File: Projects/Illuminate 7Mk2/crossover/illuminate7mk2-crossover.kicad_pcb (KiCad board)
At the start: 2 copper layers, 202.2 x 179.2 mm, 27 parts, among them J1 IN (amp), J2 TWEETER, J3 WOOFER

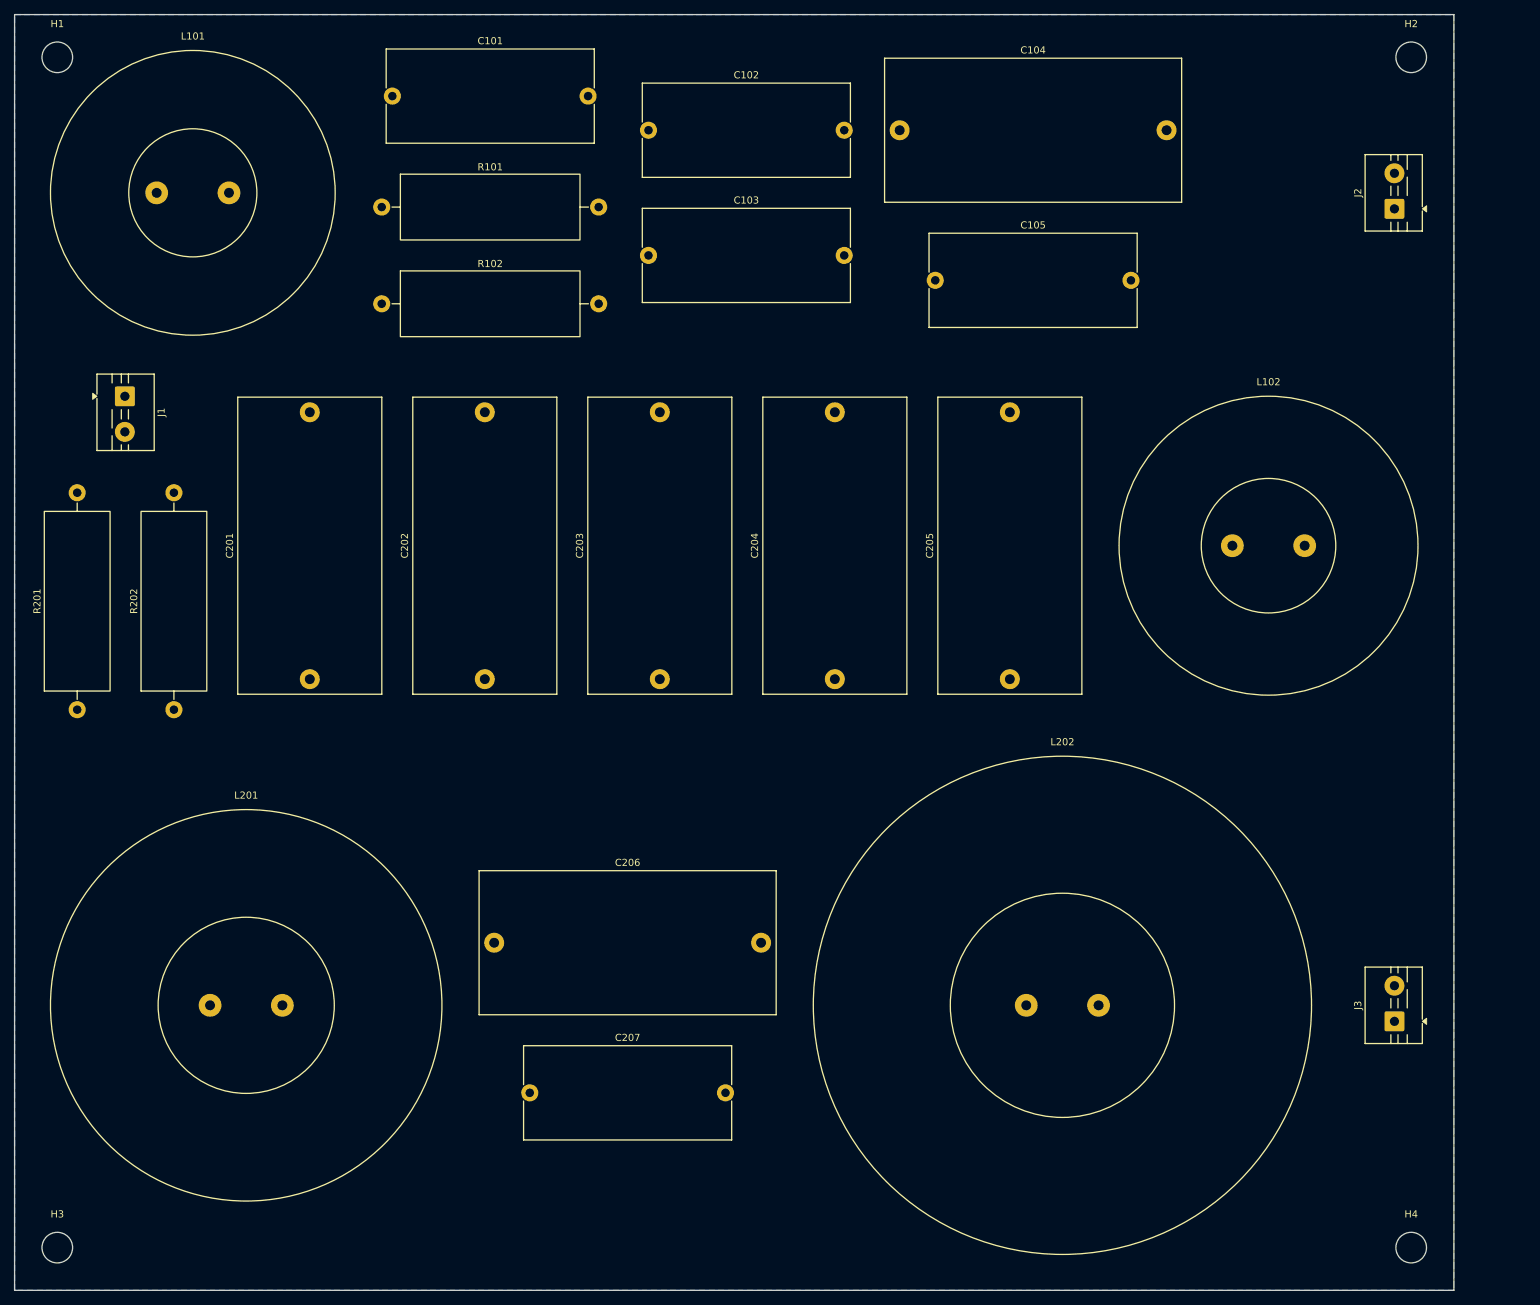
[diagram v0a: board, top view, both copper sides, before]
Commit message: Illuminate 7Mk2: crossover board shrunk to the mill envelope
Coils moved off the board: only their lead pads remain, at the edges.
Board is now 167 x 144 mm, inside the 203 x 152 mm build size.
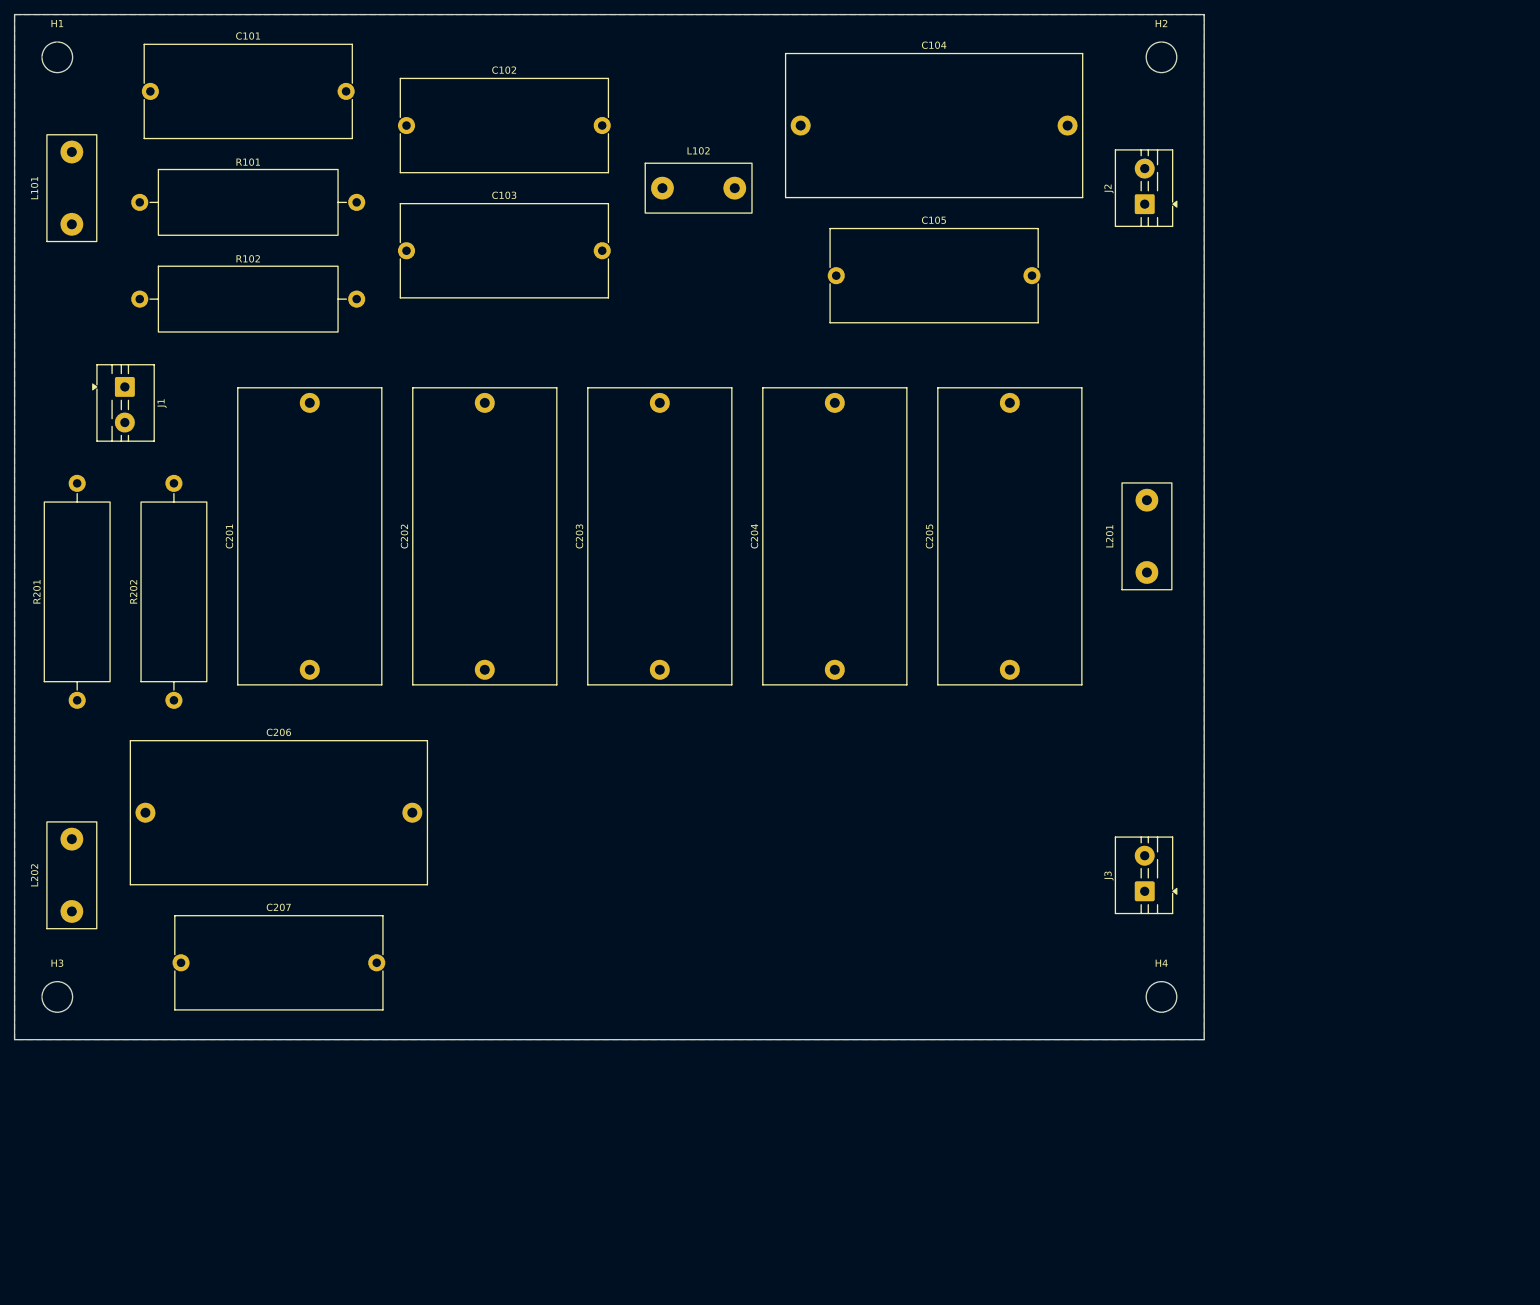
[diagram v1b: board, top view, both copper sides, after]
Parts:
- L101: footprint L_AirCore_D40mm_0.8mm -> L_OffBoard_P10.16mm
- L102: footprint L_AirCore_D42mm_0.8mm -> L_OffBoard_P10.16mm
- L201: footprint L_AirCore_D55mm_0.8mm -> L_OffBoard_P10.16mm
- L202: footprint L_AirCore_D70mm_0.8mm -> L_OffBoard_P10.16mm
- moved L201 142.7 mm to (159.1, 73.3), turned to 90 degrees
- moved L202 140.4 mm to (8.04, 120.9), turned to 90 degrees
- moved L102 94.5 mm to (96.1, 24.4)
- moved C206 52.3 mm to (18.4, 112.1)
- moved C207 52.3 mm to (23.4, 133.2)
- moved H4 49.7 mm to (161.1, 138.0)
- moved J3 39.6 mm to (158.8, 123.2)
- moved H3 35.2 mm to (6.00, 138.0)
- moved J2 35.1 mm to (158.8, 26.6)
- moved H2 35.1 mm to (161.1, 6.00)
- moved C102 34.0 mm to (55.1, 15.6)
- moved R101 34.0 mm to (17.6, 26.4)
- moved C101 34.0 mm to (19.1, 10.8)
- moved C103 34.0 mm to (55.1, 33.2)
- moved R102 34.0 mm to (17.6, 40.0)
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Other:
- board size 202.2 x 179.2 mm -> 167.1 x 144 mm

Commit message: Illuminate 7Mk2: crossover re-placed on measured shop-part footprints
All film caps, 5 W resistors and the screw terminal were measured on the
DTU shop parts and given matching stock footprints. The board re-packs to
151 x 120 mm; pcb_build.py now drops the bottom edge so the corner holes
clear every courtyard. README, handoff and BOM updated.
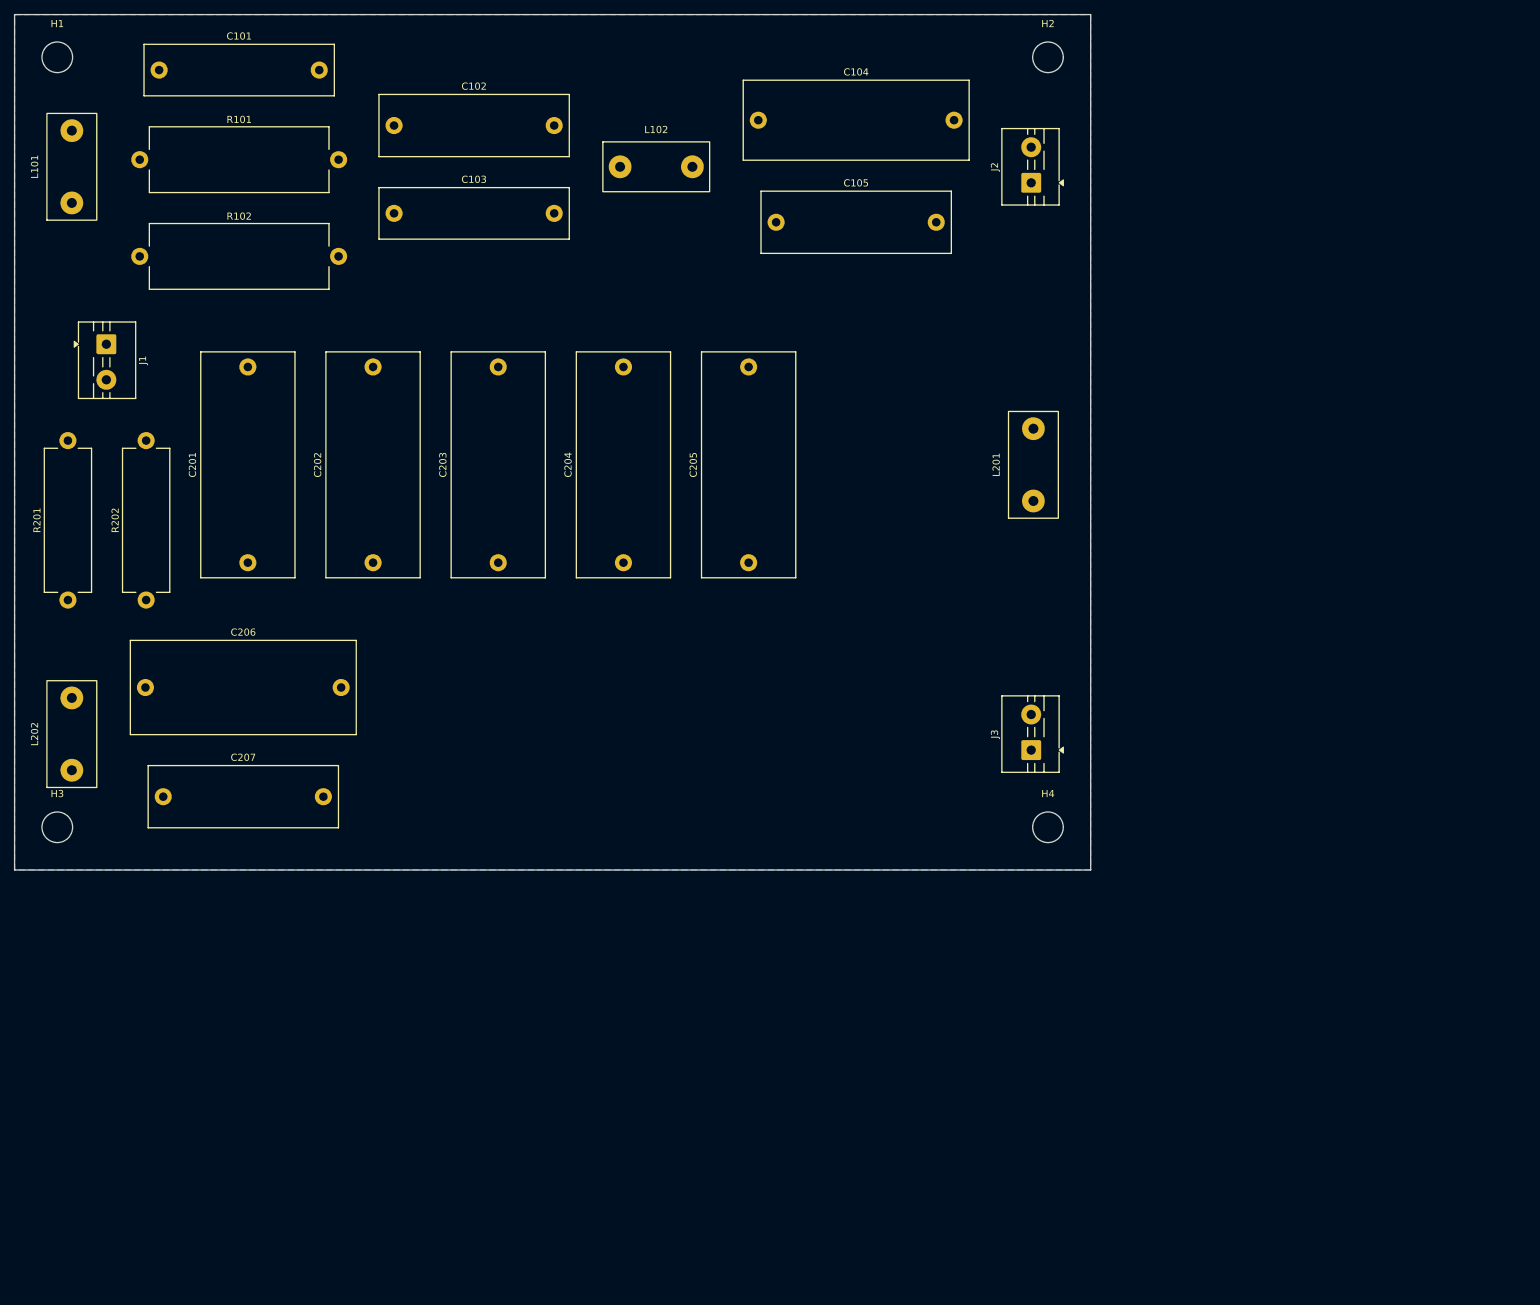
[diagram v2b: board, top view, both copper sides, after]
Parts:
- C101, C103: footprint C_Rect_L29.0mm_W13.0mm_P27.50mm_MKT -> C_Rect_L26.5mm_W7.0mm_P22.50mm_MKS4
- C102, C105, C207: footprint C_Rect_L29.0mm_W13.0mm_P27.50mm_MKT -> C_Rect_L26.5mm_W8.5mm_P22.50mm_MKS4
- C104: footprint C_Rect_L41.5mm_W20.0mm_P37.50mm_MKS4 -> C_Rect_L31.5mm_W11.0mm_P27.50mm_MKS4
- C201, C202, C203, C204, C205, C206: footprint C_Rect_L41.5mm_W20.0mm_P37.50mm_MKS4 -> C_Rect_L31.5mm_W13.0mm_P27.50mm_MKS4
- R101, R102: footprint R_Axial_Power_L25.0mm_W9.0mm_P30.48mm -> R_Axial_Power_L25.0mm_W9.0mm_P27.94mm
- R201, R202: footprint R_Axial_Power_L25.0mm_W9.0mm_P30.48mm -> R_Axial_Power_L20.0mm_W6.4mm_P22.40mm
- moved C205 39.7 mm to (103.1, 77.0)
- moved C204 33.3 mm to (85.5, 77.0)
- moved H4 28.7 mm to (145.2, 114.2)
- moved C203 27.2 mm to (68.0, 77.0)
- moved J3 25.5 mm to (142.8, 103.3)
- moved H3 23.8 mm to (6.00, 114.2)
- moved C207 23.5 mm to (20.9, 109.9)
- moved C202 21.7 mm to (50.4, 77.0)
- moved L202 19.8 mm to (8.04, 101.1)
- moved L201 18.8 mm to (143.1, 63.3)
- moved C206 17.6 mm to (18.4, 94.5)
- moved C201 17.4 mm to (32.8, 77.0)
- moved J2 16.2 mm to (142.8, 23.6)
- moved H2 15.9 mm to (145.2, 6.00)
- moved R202 14.6 mm to (18.5, 82.3)
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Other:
- board size 167.1 x 144 mm -> 151.2 x 120.2 mm

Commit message: Illuminate 7Mk2: crossover routed on B.Cu, Gerbers and laser silkscreen exported
Hand-routed single-sided on a 144.5 x 110 mm outline, M4 corner holes
re-added 6 mm in, GND pour refilled around them, silkscreen labels cleared
of the edge and of each other. DRC clean. production/ holds the Gerbers and
Excellon for the mill and the top silkscreen DXF for the laser.
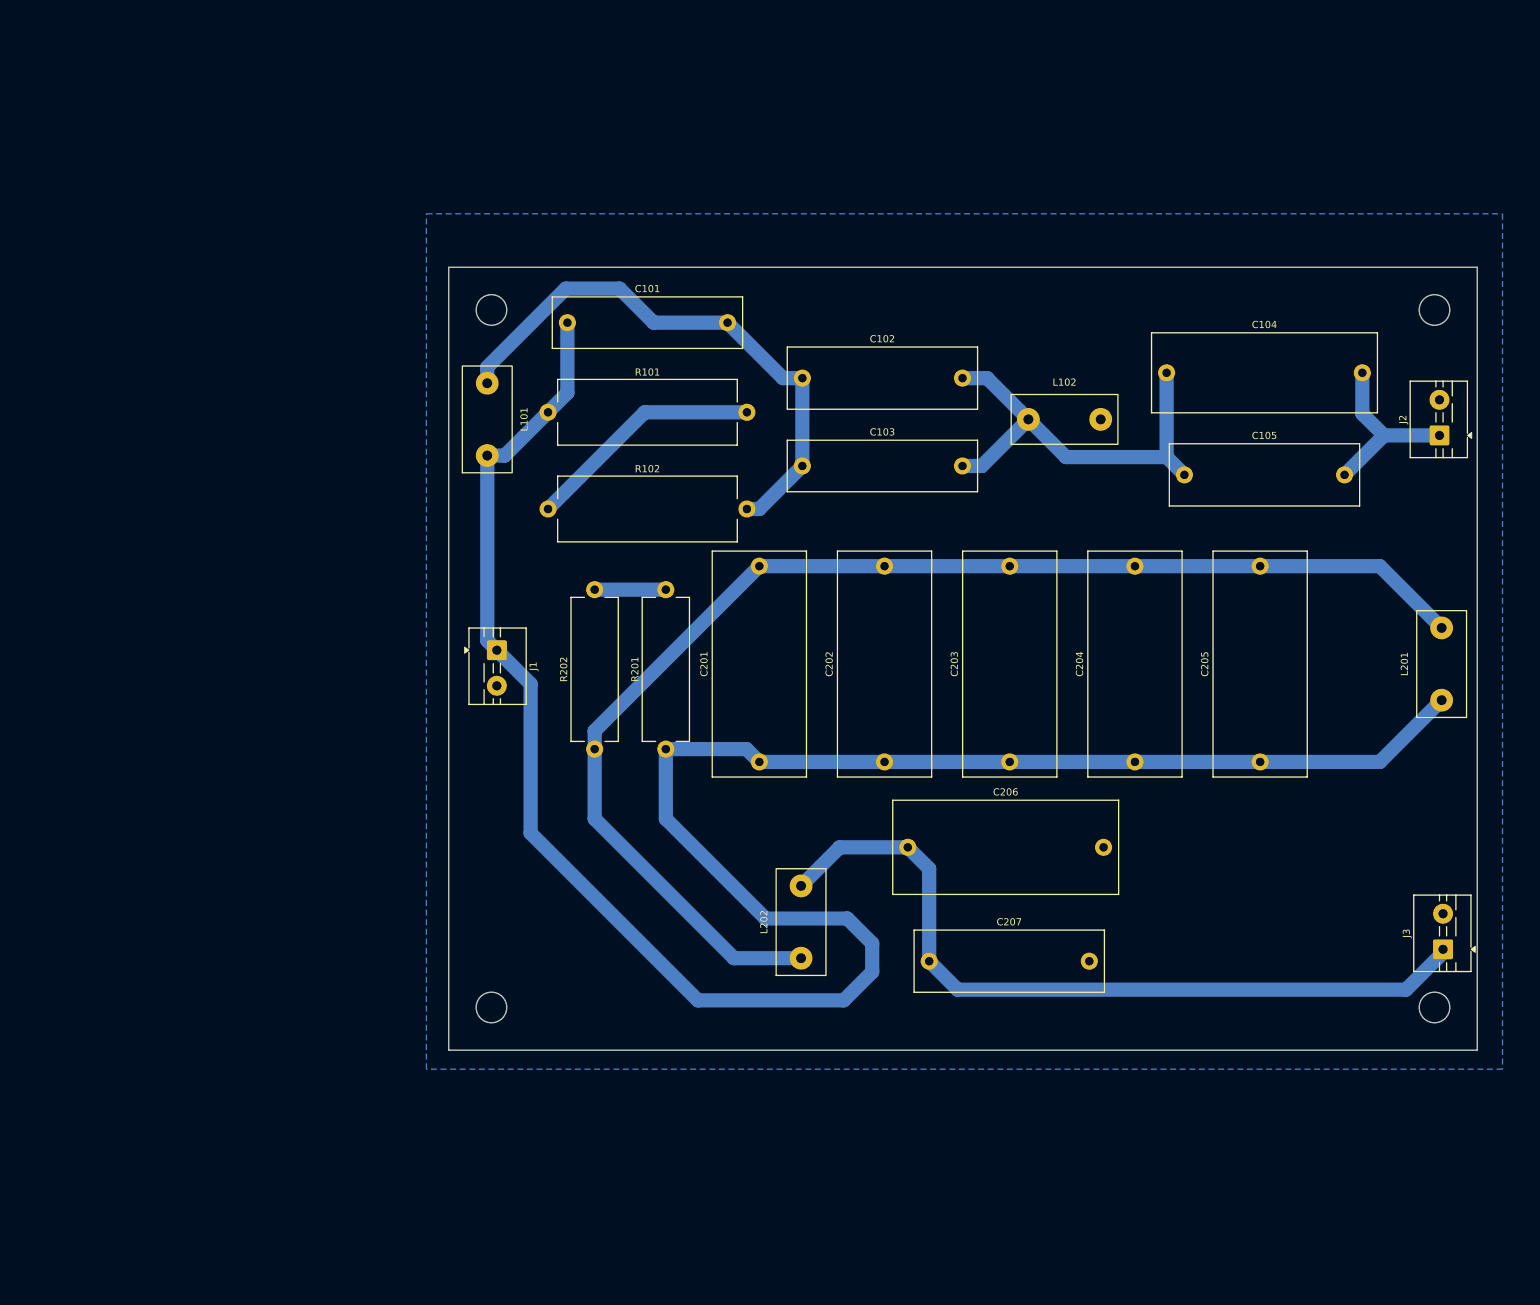
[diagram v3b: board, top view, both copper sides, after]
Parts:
- moved C207 110.1 mm to (128.5, 133.0)
- moved C206 109.4 mm to (125.5, 117.0)
- moved L202 105.8 mm to (110.5, 127.5)
- moved R201 86.6 mm to (91.5, 103.2)
- moved C201 77.1 mm to (104.6, 105.0)
- moved C202 77.1 mm to (122.2, 105.0)
- moved C203 77.1 mm to (139.8, 105.0)
- moved C204 77.1 mm to (157.4, 105.0)
- moved C205 77.1 mm to (175.0, 105.0)
- moved H1 70.6 mm to (67.0, 41.5)
- moved J1 69.7 mm to (67.8, 89.3)
- moved L101 68.3 mm to (66.4, 56.9)
- moved C102 67.5 mm to (110.7, 51.1)
- moved C103 67.5 mm to (110.7, 63.4)
- moved C104 67.5 mm to (161.9, 50.3)
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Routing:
- net /IN+: track 0.00 -> 303.1 mm
- net /WF_C: track 0.00 -> 181.6 mm
- net /WF_D: track 0.00 -> 111.0 mm
- net /TW_A: track 0.00 -> 78.9 mm
- net /TW_B: track 0.00 -> 60.6 mm
- net Net-(R101-Pad2): track 0.00 -> 33.6 mm
- net /TW+: track 0.00 -> 25.7 mm
- net Net-(R201-Pad2): track 0.00 -> 10.0 mm
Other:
- board size 151.2 x 120.2 mm -> 144.5 x 110 mm
- board text added: "SRM-20 build area 203.2 x 152.4"
- board text added: "recommended max board 189.2 x 138.4"
